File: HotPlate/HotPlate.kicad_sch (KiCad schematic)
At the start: 58 parts, among them J1 USB_C_Receptacle_USB2.0_14P, J2 Heater, Q1 PMOS_Substrate, Q2 AO3400A, SW1 RESET, SW2 BOOT, SW3 BTN0, SW4 BTN1, SW5 BTN2, SW6 BTN3, U1 RP2040, U2 USBLC6-2SC6, U3 W25Q32JVSS, U4 L78L33ACUTR, U5 HUSB238_xxxDD, U6 SSD1306, Y1 12Mhz

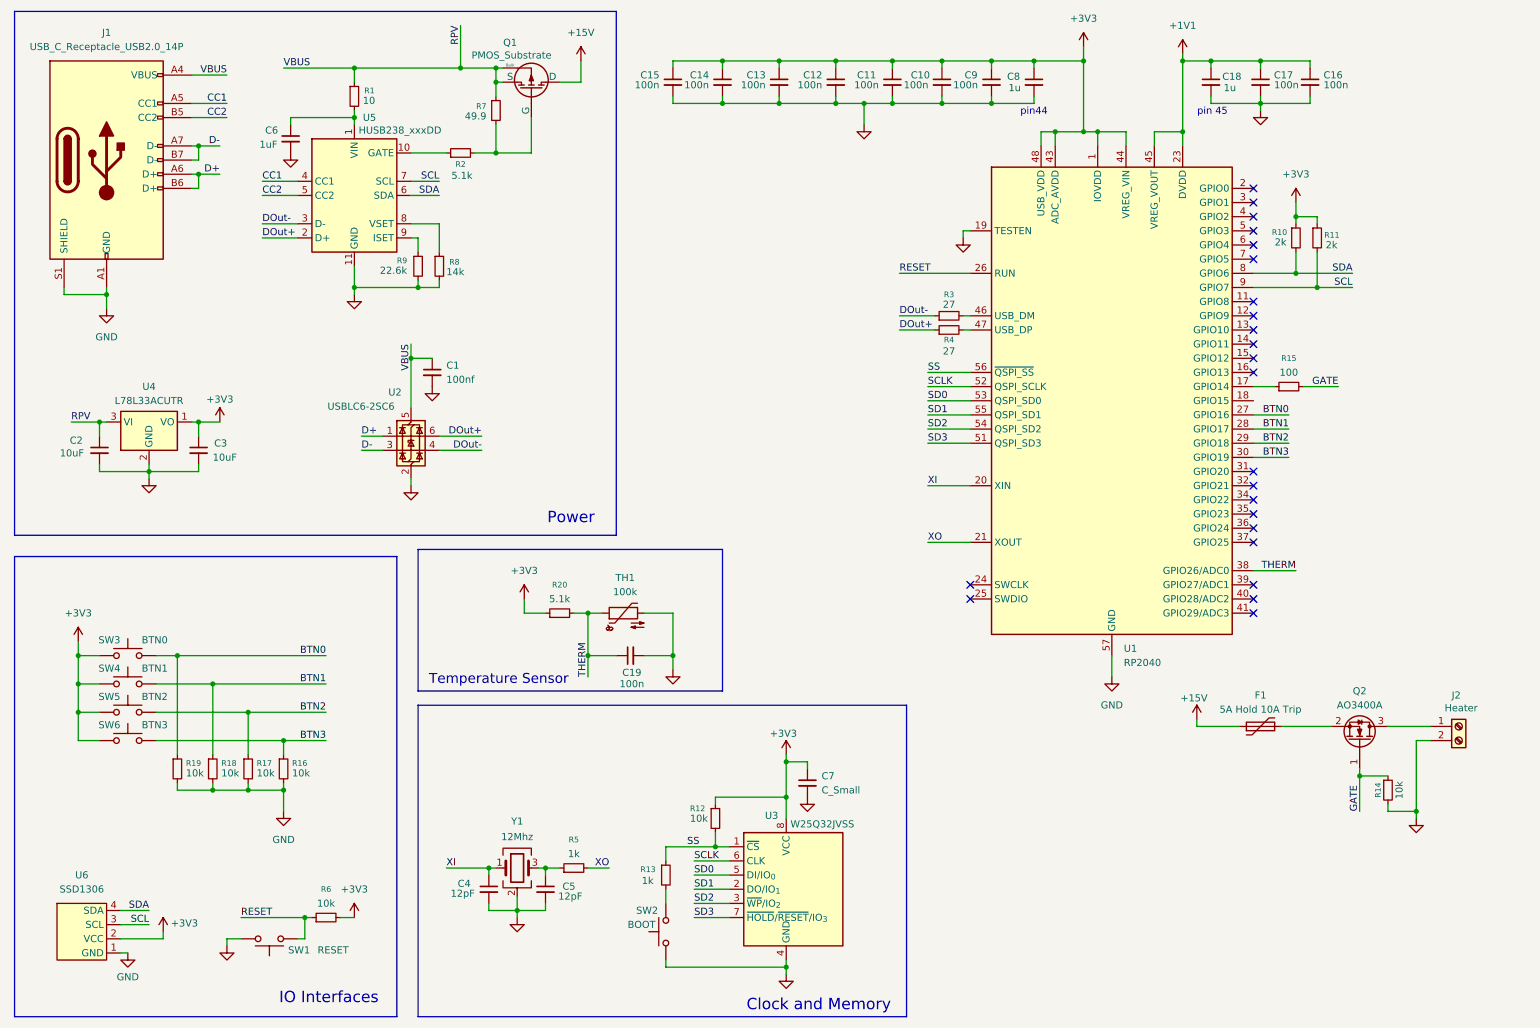
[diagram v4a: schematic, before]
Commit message: Status LEDs
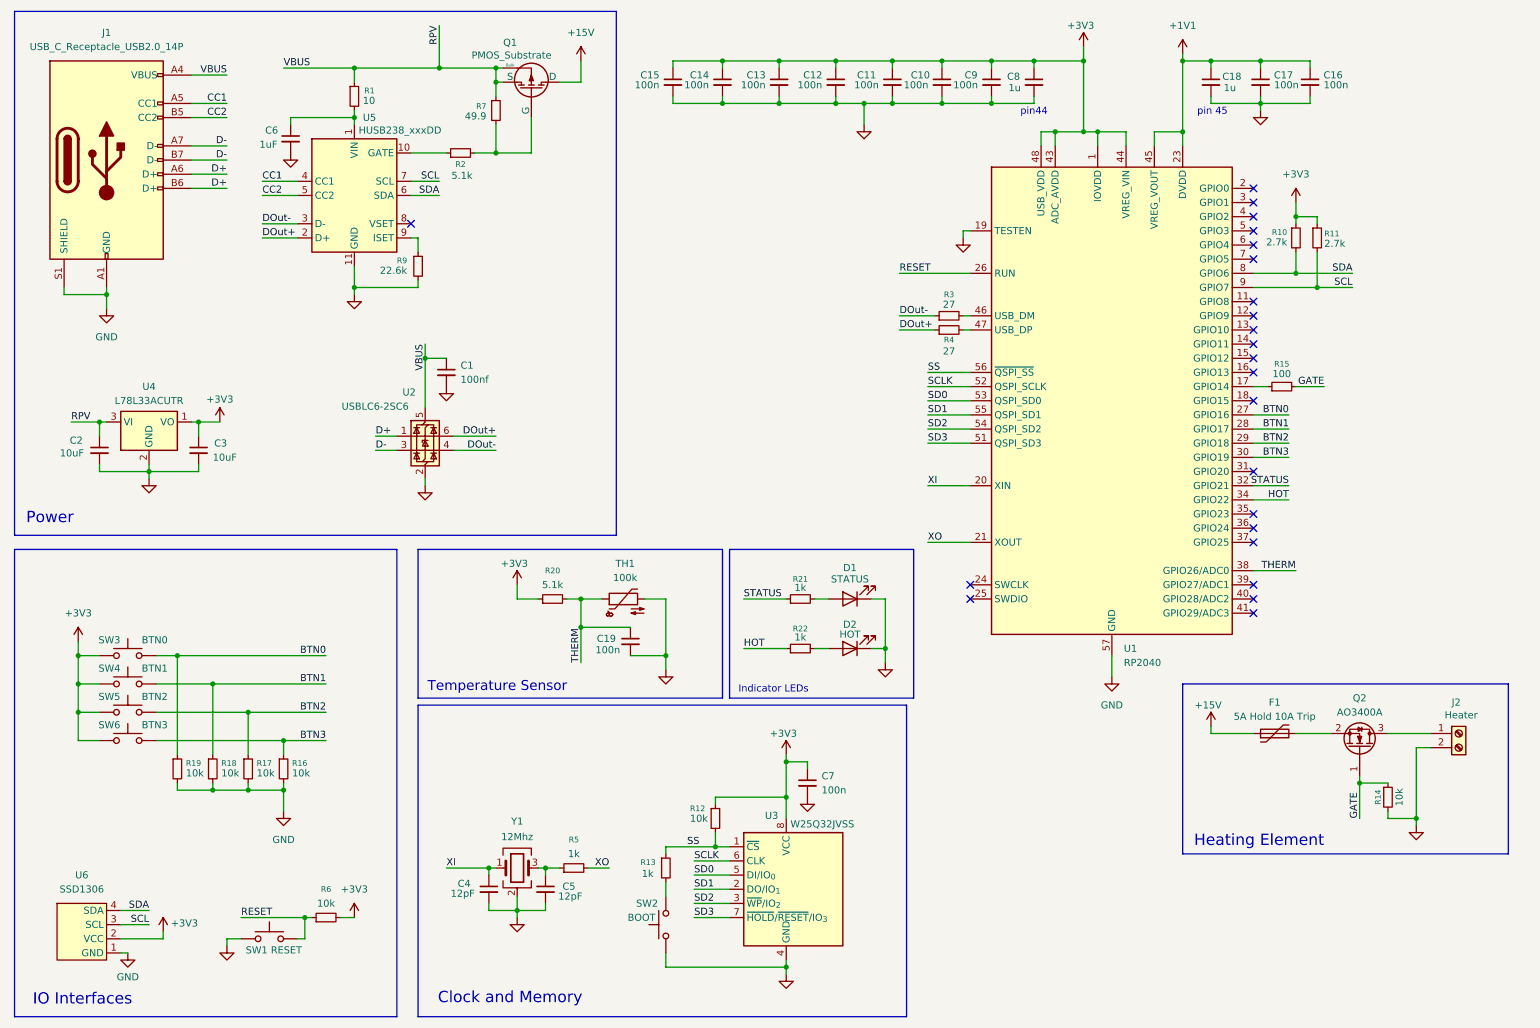
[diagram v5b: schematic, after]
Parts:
- removed R8: 14k, symbol Device:R_Small
- added D1: STATUS, symbol Device:LED
- added D2: HOT, symbol Device:LED
- added R21, R22: 1k, symbol Device:R_Small
- C7: value C_Small -> 100n
- R10, R11: value 2k -> 2.7k
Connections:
- net GND: now also SW1.1, D1.1 (K), D2.1 (K); no longer SW1.2
- net RESET: now also SW1.2; no longer SW1.1
- net STATUS: now reaches U1.32 (GPIO21)
- net STATUS: now also R21.1
- net HOT: now reaches U1.34 (GPIO22)
- net HOT: now also R22.1
- new net: D1.2 (A), R21.2
- new net: D2.2 (A), R22.2
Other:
- note added: "Heating Element"
- note added: "Indicator LEDs"
- moved on the sheet: C1, C19, F1, J2, Q2, R13, R14, R15, R20, SW1, SW2, TH1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

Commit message: Begin PCB placements and routing
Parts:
- removed Q1: PMOS_Substrate, symbol Simulation_SPICE:PMOS_Substrate
- removed Q2: AO3400A, Package_TO_SOT_SMD:SOT-23, symbol Transistor_FET:AO3400A
- added Q1: STU417S, Package_TO_SOT_SMD:TO-252-2, symbol Simulation_SPICE:PMOS
- added Q4: MS50N06, Package_TO_SOT_SMD:TO-252-2, symbol Simulation_SPICE:NMOS
- C1, C10, C11, C12, C13, C14, C15, C16, C17, C18, C19, C2, C3, C4, C5, C6, C7, C8, C9: footprint (none) -> Capacitor_SMD:C_0603_1608Metric
- D1, D2: footprint (none) -> Diode_SMD:D_0603_1608Metric
- F1: footprint (none) -> Fuse:Fuse_2920_7451Metric
- J1: footprint (none) -> Connector_USB:USB_C_Receptacle_G-Switch_GT-USB-7010ASV
- J2: footprint (none) -> TerminalBlock_Phoenix:TerminalBlock_Phoenix_PT-1,5-2-3.5-H_1x02_P3.50mm_Horizontal
- R1, R10, R11, R12, R13, R14, R15, R16, R17, R18, R19, R2, R20, R21, R22, R3, R4, R5, R6, R7, R9: footprint (none) -> Resistor_SMD:R_0603_1608Metric
- SW1, SW2: footprint (none) -> Button_Switch_SMD:SW_Push_1P1T_NO_CK_KMR2
- SW3, SW4, SW5, SW6: footprint (none) -> Button_Switch_SMD:SW_SPST_PTS647_Sx38
- TH1: footprint (none) -> Resistor_THT:R_Axial_DIN0204_L3.6mm_D1.6mm_P5.08mm_Horizontal
- U6: footprint (none) -> Connector_PinHeader_2.54mm:PinHeader_1x04_P2.54mm_Vertical
- Y1: footprint (none) -> Oscillator:Oscillator_SMD_SeikoEpson_SG8002CE-4Pin_3.2x2.5mm
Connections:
- net +15V: now also Q1.2 (D)
- net D+: now also U2.3 (I/O2); no longer U2.1 (I/O1)
- net D-: now also U2.1 (I/O1); no longer U2.3 (I/O2)
- net DOut+: now also U2.4 (I/O2); no longer U2.6 (I/O1)
- net DOut-: now also U2.6 (I/O1); no longer U2.4 (I/O2)
- net GATE: now also Q4.1 (G)
- net SCL: now also U1.37 (GPIO25); no longer U1.9 (GPIO7)
- net SDA: now also U1.36 (GPIO24); no longer U1.8 (GPIO6)
- net at F1.2: now also Q4.3 (S)
- net at R2.2, R7.2: now also Q1.1 (G)
- net at R15.1: now also U1.7 (GPIO5); no longer U1.17 (GPIO14)
- net at J2.1 (Pin_1): now also Q4.2 (D)
- net RPV renamed VBUS
- net VBUS: now also Q1.3 (S)
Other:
- moved on the sheet: R10, R11, R15, R7

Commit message: Finish routing
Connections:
- net +3V3: now also R21.1
- net BTN0: now also U1.29 (GPIO18); no longer U1.27 (GPIO16)
- net BTN1: now also U1.41 (GPIO29/ADC3); no longer U1.28 (GPIO17)
- net BTN2: now also U1.39 (GPIO27/ADC1); no longer U1.29 (GPIO18)
- net HOT: now also U1.28 (GPIO17); no longer U1.34 (GPIO22)
- net STATUS: no longer names the net of U1.32 (GPIO21)
- net STATUS: no longer R21.1
- no-connect marks 23 -> 24
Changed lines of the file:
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@@
 	)
 	(no_connect
+		(at 237.49 101.6)
+	)
+	(no_connect
+		(at 237.49 86.36)
+	)
+	(no_connect
+		(at 237.49 99.06)
+	)
+	(no_connect
 		(at 237.49 68.58)
 	)
@@
 	)
 	(no_connect
-		(at 237.49 121.92)
-	)
-	(no_connect
 		(at 237.49 45.72)
 	)
 	(no_connect
-		(at 237.49 116.84)
-	)
-	(no_connect
 		(at 237.49 53.34)
 	)
@@
 	(wire
 		(pts
+			(xy 237.49 91.44) (xy 243.84 91.44)
+		)
+		(stroke
+			(width 0)
+			(type default)
+		)
+	)
+	(wire
+		(pts
 			(xy 254 102.87) (xy 254 109.22)
 		)
@@
 	(wire
 		(pts
-			(xy 125.73 129.54) (xy 132.08 129.54)
+			(xy 237.49 116.84) (xy 243.84 116.84)
 		)
 		(stroke
@@
 	(wire
 		(pts
-			(xy 26.67 127) (xy 26.67 129.54)
+			(xy 125.73 129.54) (xy 132.08 129.54)
 		)
 		(stroke
@@
 	(wire
 		(pts
-			(xy 31.75 64.77) (xy 31.75 67.31)
+			(xy 26.67 127) (xy 26.67 129.54)
 		)
 		(stroke
@@
 	(wire
 		(pts
-			(xy 179.07 81.28) (xy 186.69 81.28)
+			(xy 31.75 64.77) (xy 31.75 67.31)
 		)
 		(stroke
@@
 	(wire
 		(pts
-			(xy 199.39 35.56) (xy 201.93 35.56)
+			(xy 179.07 81.28) (xy 186.69 81.28)
 		)
 		(stroke
@@
 	(wire
 		(pts
-			(xy 237.49 88.9) (xy 243.84 88.9)
+			(xy 199.39 35.56) (xy 201.93 35.56)
 		)
 		(stroke
@@
 	(wire
 		(pts
-			(xy 162.56 22.86) (xy 152.4 22.86)
+			(xy 237.49 121.92) (xy 243.84 121.92)
 		)
 		(stroke
@@
 	(wire
 		(pts
-			(xy 87.63 62.23) (xy 87.63 63.5)
+			(xy 162.56 22.86) (xy 152.4 22.86)
 		)
 		(stroke
@@
 	(wire
 		(pts
-			(xy 44.45 129.54) (xy 71.12 129.54)
+			(xy 87.63 62.23) (xy 87.63 63.5)
 		)
 		(stroke
@@
 	(wire
 		(pts
-			(xy 237.49 91.44) (xy 243.84 91.44)
+			(xy 44.45 129.54) (xy 71.12 129.54)
 		)
 		(stroke
@@
 	(wire
 		(pts
+			(xy 146.05 119.38) (xy 153.67 119.38)
+		)
+		(stroke
+			(width 0)
+			(type default)
+		)
+	)
+	(wire
+		(pts
 			(xy 212.09 129.54) (xy 212.09 133.35)
 		)
@@
 	(wire
 		(pts
+			(xy 237.49 88.9) (xy 243.84 88.9)
+		)
+		(stroke
+			(width 0)
+			(type default)
+		)
+	)
+	(wire
+		(pts
 			(xy 105.41 116.84) (xy 105.41 119.38)
 		)
@@
 	(wire
 		(pts
-			(xy 146.05 119.38) (xy 153.67 119.38)
-		)
-		(stroke
-			(width 0)
-			(type default)
-		)
-	)
-	(wire
-		(pts
 			(xy 26.67 129.54) (xy 26.67 134.62)
 		)
@@
 	(wire
 		(pts
-			(xy 237.49 86.36) (xy 243.84 86.36)
-		)
-		(stroke
-			(width 0)
-			(type default)
-		)
-	)
-	(wire
-		(pts
 			(xy 162.56 22.86) (xy 162.56 24.13)
 		)
@@
 	(wire
 		(pts
-			(xy 237.49 101.6) (xy 243.84 101.6)
-		)
-		(stroke
-			(width 0)
-			(type default)
-		)
-	)
-	(wire
-		(pts
 			(xy 173.99 68.58) (xy 180.34 68.58)
 		)
@@
 	(wire
 		(pts
+			(xy 146.05 118.11) (xy 146.05 119.38)
+		)
+		(stroke
+			(width 0)
+			(type default)
+		)
+	)
+	(wire
+		(pts
 			(xy 250.19 102.87) (xy 250.19 106.68)
 		)
@@
 	(wire
 		(pts
-			(xy 237.49 99.06) (xy 243.84 99.06)
-		)
-		(stroke
-			(width 0)
-			(type default)
-		)
-	)
-	(wire
-		(pts
 			(xy 41.91 180.34) (xy 41.91 179.07)
 		)
@@
 	)
 	(label "BTN1"
-		(at 243.84 88.9 180)
+		(at 243.84 121.92 180)
 		(effects
 			(font
@@
 	)
 	(label "HOT"
-		(at 243.84 101.6 180)
+		(at 243.84 88.9 180)
 		(effects
 			(font
@@
 	)
 	(label "BTN0"
-		(at 243.84 86.36 180)
+		(at 243.84 91.44 180)
 		(effects
 			(font
@@
 		)
 	)
-	(label "STATUS"
-		(at 243.84 99.06 180)
-		(effects
-			(font
-				(size 1.27 1.27)
-			)
-			(justify right bottom)
-		)
-	)
 	(label "SCL"
 		(at 39.37 177.8 180)
@@
 	)
 	(label "BTN2"
-		(at 243.84 91.44 180)
+		(at 243.84 116.84 180)
 		(effects
 			(font
@@
 		)
 	)
-	(label "STATUS"
-		(at 146.05 119.38 0)
-		(effects
-			(font
-				(size 1.27 1.27)
-			)
-			(justify left bottom)
-		)
-	)
 	(label "RESET"
 		(at 55.88 176.53 0)
@@
 					(unit 1)
 				)
+			)
+		)
+	)
+	(symbol
+		(lib_id "power:+3V3")
+		(at 146.05 118.11 0)
+		(unit 1)
+		(exclude_from_sim no)
+		(in_bom yes)
+		(on_board yes)
+		(dnp no)
+		(property "Reference" "#PWR031"
+			(at 146.05 121.92 0)
+			(effects
+				(font
+					(size 1.27 1.27)
+				)
+				(hide yes)
+			)
+		)
+		(property "Value" "+3V3"
+			(at 146.558 114.046 0)
+			(effects
+				(font
+					(size 1.27 1.27)
+				)
+			)
+		)
+		(property "Footprint" ""
+			(at 146.05 118.11 0)
+			(effects
+				(font
+					(size 1.27 1.27)
+				)
+				(hide yes)
+			)
+		)
+		(property "Datasheet" ""
+			(at 146.05 118.11 0)
+			(effects
+				(font
+					(size 1.27 1.27)
+				)
+				(hide yes)
+			)
+		)
+		(property "Description" "Power symbol creates a global label with name \"+3V3\""
+			(at 146.05 118.11 0)
+			(effects
+				(font
+					(size 1.27 1.27)
+				)
+				(hide yes)
+			)
+		)
+		(pin "1"
+		)
+		(instances
+			(project ""
+				(path "/cd7b1ccb-f245-4cda-a4ed-50660074b2f5"
+					(reference "#PWR031")
+					(unit 1)
+				)
